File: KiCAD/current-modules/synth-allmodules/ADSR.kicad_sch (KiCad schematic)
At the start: 39 parts, among them Q1 BC547, Q2 BC547, Q3 BC547, Q4 BC547, SW1 SW_Push, U1 ICM7555xP, U2 TL074

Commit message: Resumed ADSR
Additions:
- Annotated some of the ADSR and added some connections
Changes:
- None
Removals:
- None
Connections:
- net GND: now also C2.2
- net at R13.1: now also U2.9 (-)
- net at R13.2: now also R14.2, U2.6 (-)
- net at RV2.1: now also C2.1, RV3.1, RV4.1, U2.10 (+)
- net at U1.3 (OUT): now also D5.2 (A)
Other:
- note added: "attack"
- note added: "decay"
- note added: "gate in"
- note added: "release"
- note added: "trig"
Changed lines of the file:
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@@
 	(generator_version "10.0")
 	(paper "A4")
+	(text "trig"
+		(exclude_from_sim no)
+		(at 20.066 42.926 0)
+		(effects
+			(font
+				(size 1.27 1.27)
+			)
+		)
+	)
+	(text "attack"
+		(exclude_from_sim no)
+		(at 159.258 154.686 0)
+		(effects
+			(font
+				(size 1.27 1.27)
+			)
+		)
+	)
+	(text "release"
+		(exclude_from_sim no)
+		(at 159.766 131.064 0)
+		(effects
+			(font
+				(size 1.27 1.27)
+			)
+		)
+	)
+	(text "gate in"
+		(exclude_from_sim no)
+		(at 35.814 57.15 0)
+		(effects
+			(font
+				(size 1.27 1.27)
+			)
+		)
+	)
+	(text "decay"
+		(exclude_from_sim no)
+		(at 161.036 86.106 0)
+		(effects
+			(font
+				(size 1.27 1.27)
+			)
+		)
+	)
+	(junction
+		(at 165.1 129.54)
+		(diameter 0)
+		(color 0 0 0 0)
+	)
 	(junction
 		(at 134.62 50.8)
@@
 	)
 	(junction
+		(at 165.1 134.62)
+		(diameter 0)
+		(color 0 0 0 0)
+	)
+	(junction
 		(at 149.86 134.62)
 		(diameter 0)
@@
 	)
 	(junction
+		(at 165.1 158.75)
+		(diameter 0)
+		(color 0 0 0 0)
+	)
+	(junction
+		(at 177.8 86.36)
+		(diameter 0)
+		(color 0 0 0 0)
+	)
+	(junction
 		(at 68.58 49.53)
 		(diameter 0)
@@
 	(wire
 		(pts
+			(xy 165.1 134.62) (xy 165.1 129.54)
+		)
+		(stroke
+			(width 0)
+			(type default)
+		)
+	)
+	(wire
+		(pts
+			(xy 106.68 158.75) (xy 86.36 158.75)
+		)
+		(stroke
+			(width 0)
+			(type default)
+		)
+	)
+	(wire
+		(pts
 			(xy 96.52 48.26) (xy 96.52 50.8)
 		)
@@
 	(wire
 		(pts
+			(xy 86.36 120.65) (xy 81.28 120.65)
+		)
+		(stroke
+			(width 0)
+			(type default)
+		)
+	)
+	(wire
+		(pts
 			(xy 68.58 48.26) (xy 68.58 49.53)
 		)
@@
 	(wire
 		(pts
+			(xy 165.1 90.17) (xy 160.02 90.17)
+		)
+		(stroke
+			(width 0)
+			(type default)
+		)
+	)
+	(wire
+		(pts
 			(xy 106.68 57.15) (xy 106.68 50.8)
 		)
@@
 	(wire
 		(pts
+			(xy 86.36 158.75) (xy 86.36 120.65)
+		)
+		(stroke
+			(width 0)
+			(type default)
+		)
+	)
+	(wire
+		(pts
 			(xy 114.3 57.15) (xy 115.57 57.15)
 		)
@@
 	(wire
 		(pts
+			(xy 165.1 129.54) (xy 181.61 129.54)
+		)
+		(stroke
+			(width 0)
+			(type default)
+		)
+	)
+	(wire
+		(pts
 			(xy 137.16 134.62) (xy 139.7 134.62)
 		)
@@
 	(wire
 		(pts
+			(xy 160.02 134.62) (xy 165.1 134.62)
+		)
+		(stroke
+			(width 0)
+			(type default)
+		)
+	)
+	(wire
+		(pts
 			(xy 127 144.78) (xy 129.54 144.78)
 		)
@@
 	(wire
 		(pts
+			(xy 165.1 129.54) (xy 165.1 90.17)
+		)
+		(stroke
+			(width 0)
+			(type default)
+		)
+	)
+	(wire
+		(pts
 			(xy 60.96 115.57) (xy 49.53 115.57)
 		)
@@
 	(wire
 		(pts
+			(xy 165.1 160.02) (xy 165.1 158.75)
+		)
+		(stroke
+			(width 0)
+			(type default)
+		)
+	)
+	(wire
+		(pts
 			(xy 134.62 48.26) (xy 134.62 50.8)
 		)
@@
 	(wire
 		(pts
+			(xy 165.1 158.75) (xy 165.1 134.62)
+		)
+		(stroke
+			(width 0)
+			(type default)
+		)
+	)
+	(wire
+		(pts
 			(xy 46.99 125.73) (xy 46.99 85.09)
 		)
@@
 	(wire
 		(pts
+			(xy 196.85 76.2) (xy 177.8 76.2)
+		)
+		(stroke
+			(width 0)
+			(type default)
+		)
+	)
+	(wire
+		(pts
 			(xy 50.8 38.1) (xy 48.26 38.1)
 		)
@@
 	(wire
 		(pts
+			(xy 181.61 124.46) (xy 177.8 124.46)
+		)
+		(stroke
+			(width 0)
+			(type default)
+		)
+	)
+	(wire
+		(pts
 			(xy 156.21 162.56) (xy 149.86 162.56)
 		)
@@
 	(wire
 		(pts
+			(xy 177.8 124.46) (xy 177.8 102.87)
+		)
+		(stroke
+			(width 0)
+			(type default)
+		)
+	)
+	(wire
+		(pts
 			(xy 111.76 134.62) (xy 137.16 134.62)
 		)
@@
 	(wire
 		(pts
+			(xy 177.8 86.36) (xy 177.8 95.25)
+		)
+		(stroke
+			(width 0)
+			(type default)
+		)
+	)
+	(wire
+		(pts
 			(xy 114.3 158.75) (xy 139.7 158.75)
 		)
@@
 	(wire
 		(pts
+			(xy 160.02 158.75) (xy 165.1 158.75)
+		)
+		(stroke
+			(width 0)
+			(type default)
+		)
+	)
+	(wire
+		(pts
+			(xy 177.8 76.2) (xy 177.8 86.36)
+		)
+		(stroke
+			(width 0)
+			(type default)
+		)
+	)
+	(wire
+		(pts
 			(xy 106.68 82.55) (xy 106.68 57.15)
 		)
@@
 	(wire
 		(pts
+			(xy 194.31 86.36) (xy 177.8 86.36)
+		)
+		(stroke
+			(width 0)
+			(type default)
+		)
+	)
+	(wire
+		(pts
 			(xy 149.86 90.17) (xy 152.4 90.17)
 		)
@@
 		)
 		(stroke
+			(width 0)
+			(type default)
+		)
+	)
+	(wire
+		(pts
+			(xy 165.1 167.64) (xy 165.1 172.72)
+		)
+		(stroke

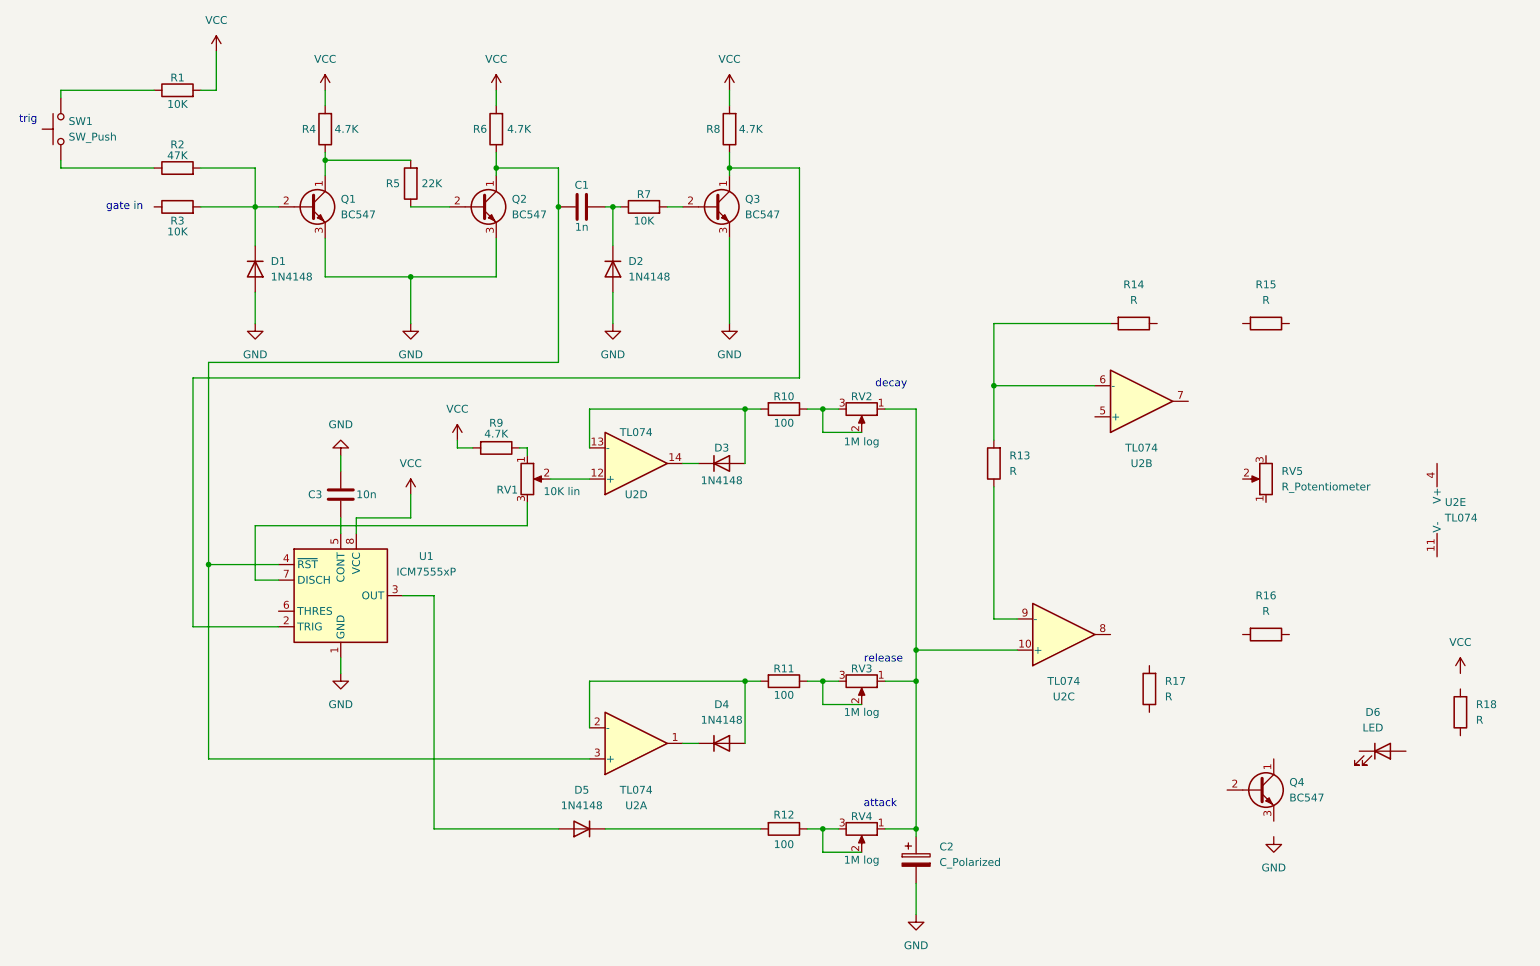
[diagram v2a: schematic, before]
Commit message: ADSR Work (Needs cap values)
Additions:
- Remaining ADSR annotations
- Remaining ADSR connections
- Remaining ADSR components
Changes:
- None
Removals:
- None
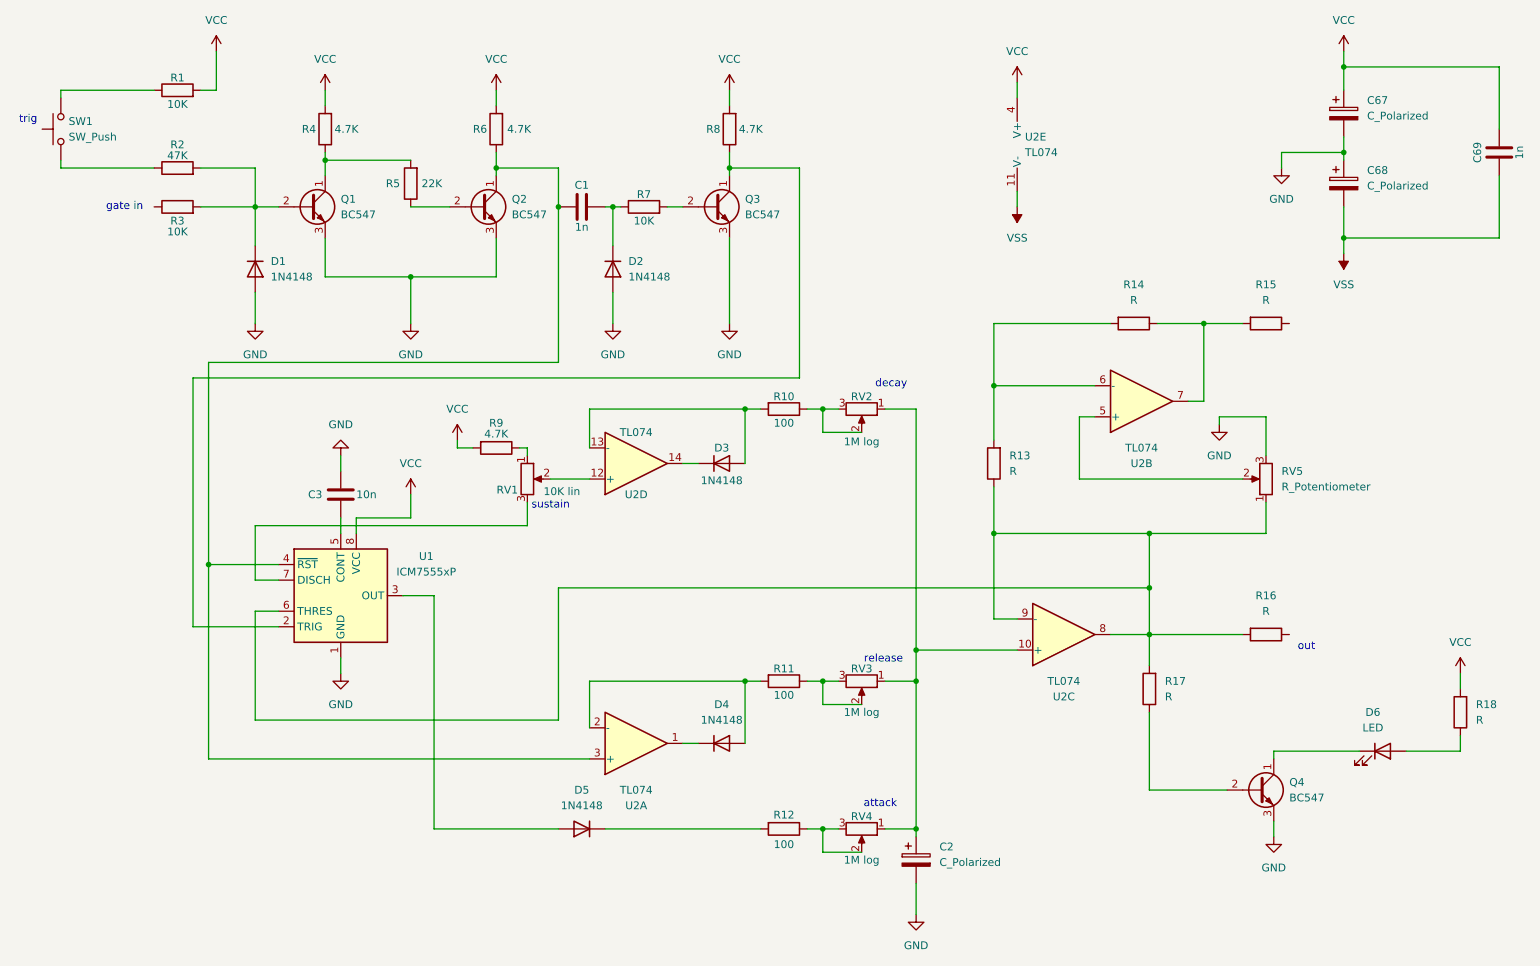
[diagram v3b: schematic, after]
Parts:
- added C67, C68: C_Polarized, symbol Device:C_Polarized
- added C69: 1n, symbol Device:C
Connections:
- net GND: now also Q4.3 (E), RV5.3, C67.2, C68.1
- net VCC: now also R18.2, U2.4 (V+), C67.1, C69.2
- net at R15.2: now also R14.1, U2.7
- net at Q4.1 (C): now also D6.1 (K)
- net at Q4.2 (B): now also R17.1
- net at R13.1, U2.9 (-): now also R16.2, R17.2, RV5.1, U1.6 (THRES), U2.8
- net VSS: now reaches U2.11 (V-)
- net VSS: now also C68.2, C69.1
- net at D6.2 (A): now also R18.1
- net at U2.5 (+): now also RV5.2
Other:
- note added: "out"
- note added: "sustain"
- moved on the sheet: U2E
